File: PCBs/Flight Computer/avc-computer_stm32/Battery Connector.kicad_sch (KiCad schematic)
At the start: 3 parts, among them J2 Battery Connector, J4 ESC Power

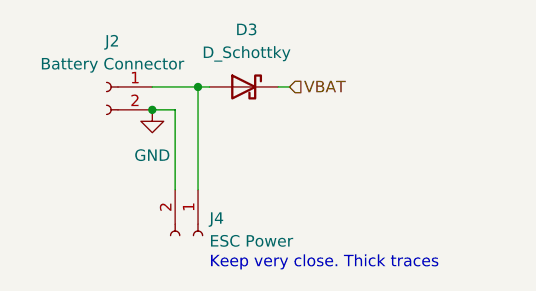
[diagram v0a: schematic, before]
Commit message: Began fixing reference designators
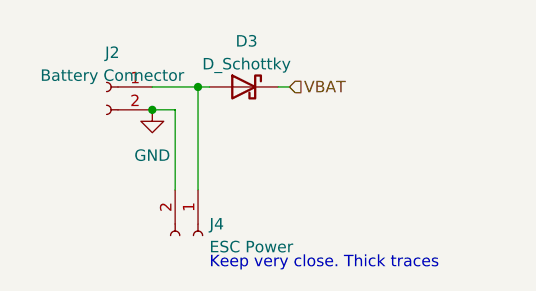
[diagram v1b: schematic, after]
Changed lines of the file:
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@@
   (symbol (lib_id "power:GND") (at 143.51 82.55 0) (unit 1)
     (in_bom yes) (on_board yes) (dnp no) (fields_autoplaced)
-    (property "Reference" "#PWR0150" (at 143.51 88.9 0)
+    (property "Reference" "#PWR041" (at 143.51 88.9 0)
       (effects (font (size 1.27 1.27)) hide)
     )
@@
       (project "avc-computer"
         (path "/e63e39d7-6ac0-4ffd-8aa3-1841a4541b55/feb67fac-24a5-46c8-b058-e8d08103a624"
-          (reference "#PWR0150") (unit 1)
+          (reference "#PWR041") (unit 1)
         )
       )
@@
   (symbol (lib_id "Device:D_Schottky") (at 153.67 80.01 0) (mirror y) (unit 1)
     (in_bom yes) (on_board yes) (dnp no) (fields_autoplaced)
-    (property "Reference" "D3" (at 153.9875 73.66 0)
+    (property "Reference" "D3" (at 153.9875 74.93 0)
       (effects (font (size 1.27 1.27)))
     )
-    (property "Value" "D_Schottky" (at 153.9875 76.2 0)
+    (property "Value" "D_Schottky" (at 153.9875 77.47 0)
       (effects (font (size 1.27 1.27)))
     )
@@
   (symbol (lib_id "Connector:Conn_01x02_Female") (at 138.43 80.01 0) (mirror y) (unit 1)
     (in_bom yes) (on_board yes) (dnp no) (fields_autoplaced)
-    (property "Reference" "J2" (at 139.065 74.93 0)
+    (property "Reference" "J2" (at 139.065 76.2 0)
       (effects (font (size 1.27 1.27)))
     )
-    (property "Value" "Battery Connector" (at 139.065 77.47 0)
+    (property "Value" "Battery Connector" (at 139.065 78.74 0)
       (effects (font (size 1.27 1.27)))
     )
@@
   (symbol (lib_id "Connector:Conn_01x02_Female") (at 148.59 96.52 270) (unit 1)
     (in_bom yes) (on_board yes) (dnp no) (fields_autoplaced)
-    (property "Reference" "J4" (at 149.86 94.6149 90)
+    (property "Reference" "J4" (at 149.86 95.25 90)
       (effects (font (size 1.27 1.27)) (justify left))
     )
-    (property "Value" "ESC Power" (at 149.86 97.1549 90)
+    (property "Value" "ESC Power" (at 149.86 97.79 90)
       (effects (font (size 1.27 1.27)) (justify left))
     )
